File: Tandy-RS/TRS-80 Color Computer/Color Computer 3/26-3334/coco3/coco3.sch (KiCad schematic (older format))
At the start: 5 parts, among them CN1 Conn_02x20_Odd_Even

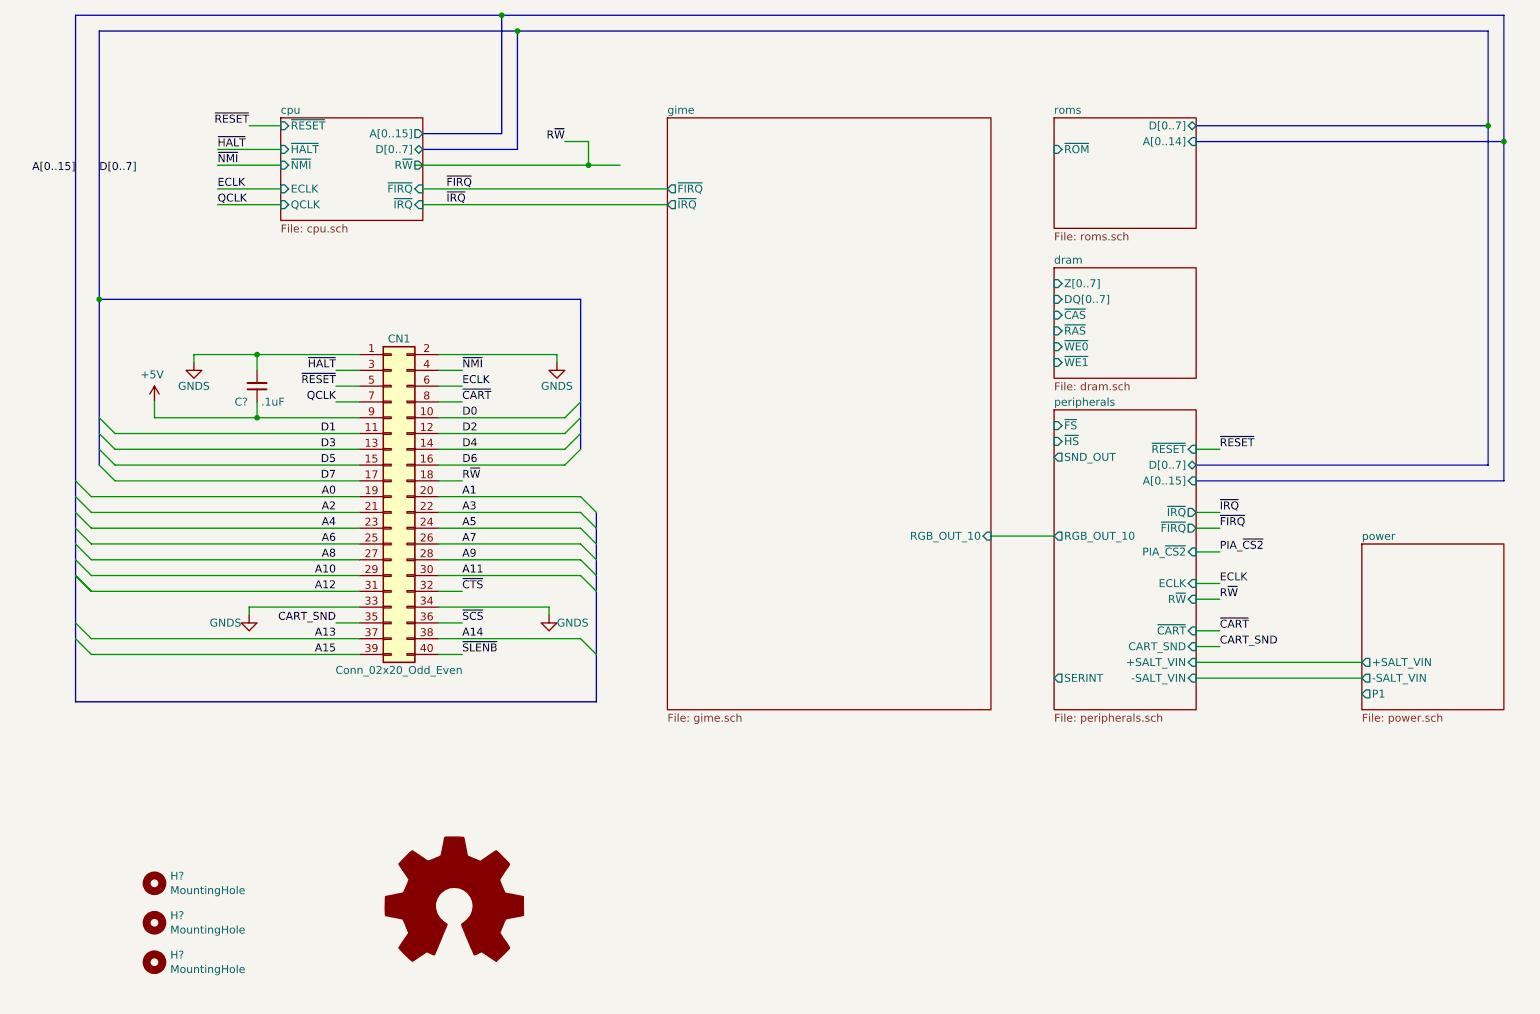
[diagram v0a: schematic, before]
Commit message: finished GIME section
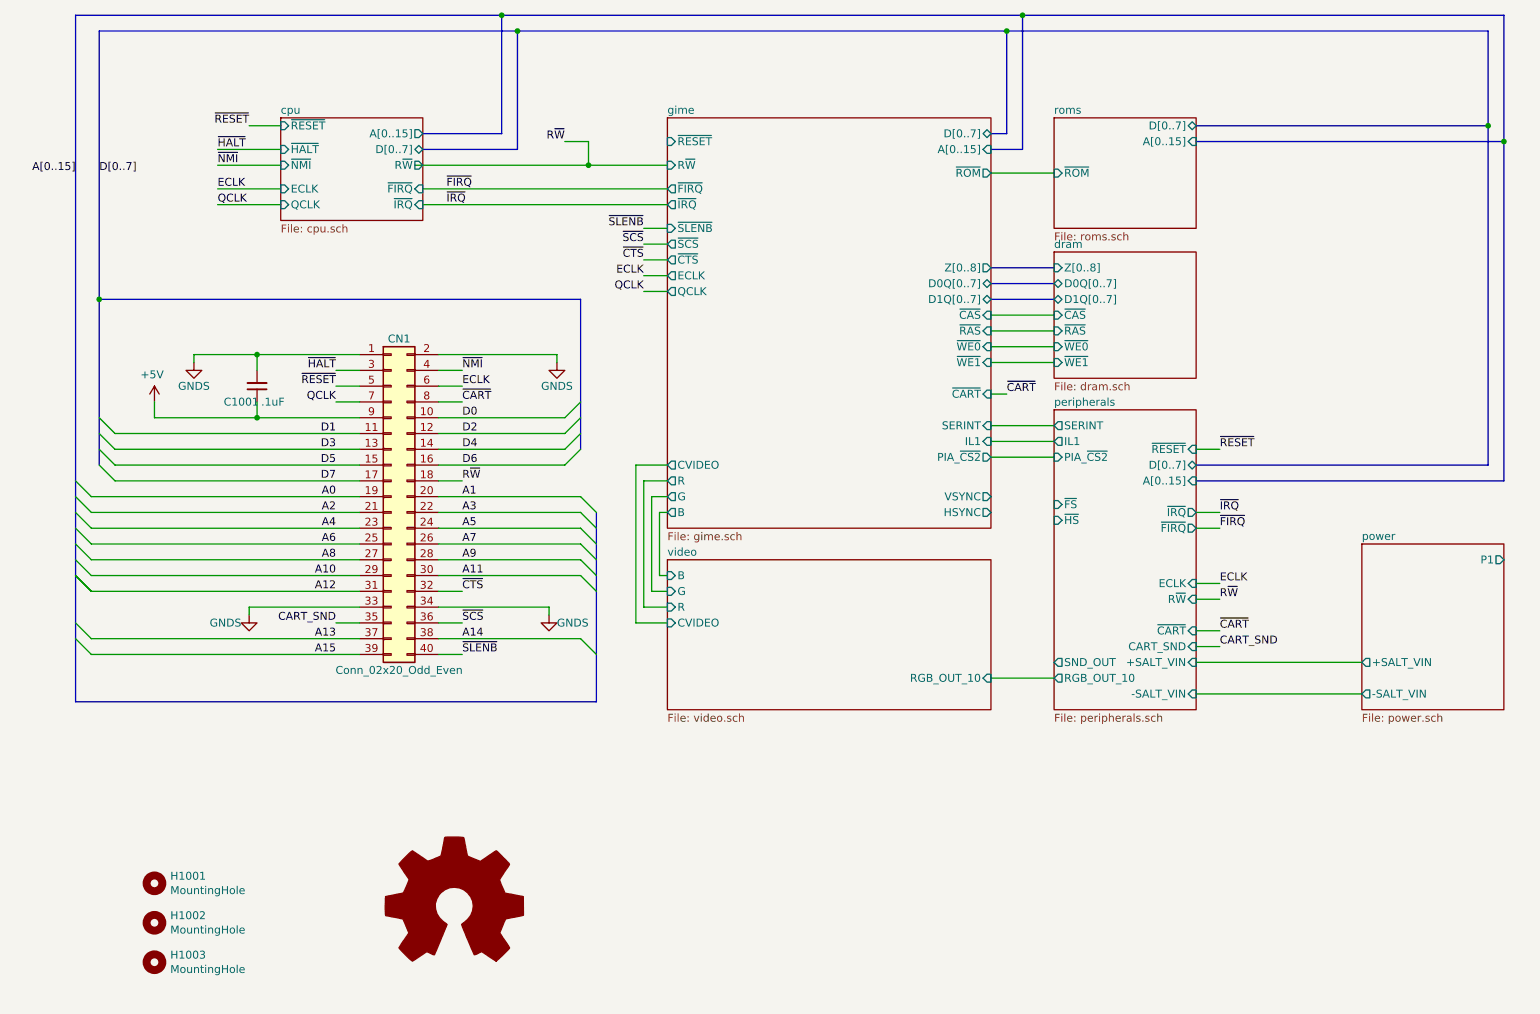
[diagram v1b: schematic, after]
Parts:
- gave numbers to parts that had none: 4
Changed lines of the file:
@@
 $Descr A 11000 8500
 encoding utf-8
-Sheet 1 7
+Sheet 1 8
 Title "TRS-80 Color Computer 3 (26-3334)"
 Date "2021-07-06"
@@
 $EndDescr
 $Sheet
-S 7050 3050 900  700
+S 7050 2950 900  800
 U 603E4732
 F0 "dram" 50
@@
 F2 "~RAS" I L 7050 3450 50
 F3 "~CAS" I L 7050 3350 50
-F4 "DQ[0..7]" I L 7050 3250 50
-F5 "Z[0..7]" I L 7050 3150 50
-F6 "~WE0" I L 7050 3550 50
-F7 "~WE1" I L 7050 3650 50
+F4 "~WE0" I L 7050 3550 50
+F5 "~WE1" I L 7050 3650 50
+F6 "Z[0..8]" I L 7050 3050 50
+F7 "D0Q[0..7]" B L 7050 3150 50
+F8 "D1Q[0..7]" B L 7050 3250 50
 $EndSheet
 $Sheet
@@
 F0 "roms" 50
 F1 "roms.sch" 50
-F2 "A[0..14]" I R 7950 2250 50
-F3 "D[0..7]" B R 7950 2150 50
-F4 "~ROM" I L 7050 2300 50
+F2 "D[0..7]" B R 7950 2150 50
+F3 "~ROM" I L 7050 2450 50
+F4 "A[0..15]" I R 7950 2250 50
 $EndSheet
 $Sheet
@@
 AR Path="/603E4732/60A48794" Ref="#PWR?"  Part="1"
 AR Path="/603D345E/60A48794" Ref="#PWR?"  Part="1"
-AR Path="/60A48794" Ref="#PWR?"  Part="1"
-F 0 "#PWR?" H 1600 3400 50  0001 C CNN
+AR Path="/60A48794" Ref="#PWR01001"  Part="1"
+F 0 "#PWR01001" H 1600 3400 50  0001 C CNN
 F 1 "GNDS" H 1600 3500 50  0000 C CNN
 F 2 "" H 1600 3650 50  0001 C CNN
@@
 AR Path="/603E4732/60A3AC34" Ref="#PWR?"  Part="1"
 AR Path="/603D345E/60A3AC34" Ref="#PWR?"  Part="1"
-AR Path="/60A3AC34" Ref="#PWR?"  Part="1"
-F 0 "#PWR?" H 3900 3400 50  0001 C CNN
+AR Path="/60A3AC34" Ref="#PWR01002"  Part="1"
+F 0 "#PWR01002" H 3900 3400 50  0001 C CNN
 F 1 "GNDS" H 3900 3500 50  0000 C CNN
 F 2 "" H 3900 3650 50  0001 C CNN
@@
 AR Path="/603E4732/60A24DD1" Ref="#PWR?"  Part="1"
 AR Path="/603D345E/60A24DD1" Ref="#PWR?"  Part="1"
-AR Path="/60A24DD1" Ref="#PWR?"  Part="1"
-F 0 "#PWR?" H 3850 5000 50  0001 C CNN
+AR Path="/60A24DD1" Ref="#PWR01005"  Part="1"
+F 0 "#PWR01005" H 3850 5000 50  0001 C CNN
 F 1 "GNDS" H 3700 5200 50  0000 C CNN
 F 2 "" H 3850 5250 50  0001 C CNN
@@
 AR Path="/603E4732/60A1FE63" Ref="#PWR?"  Part="1"
 AR Path="/603D345E/60A1FE63" Ref="#PWR?"  Part="1"
-AR Path="/60A1FE63" Ref="#PWR?"  Part="1"
-F 0 "#PWR?" H 1950 5000 50  0001 C CNN
+AR Path="/60A1FE63" Ref="#PWR01004"  Part="1"
+F 0 "#PWR01004" H 1950 5000 50  0001 C CNN
 F 1 "GNDS" H 1800 5200 50  0000 C CNN
 F 2 "" H 1950 5250 50  0001 C CNN
@@
 P 2000 3800
 AR Path="/60273794/6093C001" Ref="C?"  Part="1"
-AR Path="/6093C001" Ref="C?"  Part="1"
-F 0 "C?" H 2100 3900 50  0000 C CNN
+AR Path="/6093C001" Ref="C1001"  Part="1"
+F 0 "C1001" H 2100 3900 50  0000 C CNN
 F 1 ".1uF" H 1900 3900 50  0000 C CNN
 F 2 "Capacitor_THT:C_Disc_D4.7mm_W2.5mm_P5.00mm" H 2000 3800 50  0001 C CNN
@@
 P 1350 3900
 AR Path="/60273794/6093BFF7" Ref="#PWR?"  Part="1"
-AR Path="/6093BFF7" Ref="#PWR?"  Part="1"
-F 0 "#PWR?" H 1350 3750 50  0001 C CNN
+AR Path="/6093BFF7" Ref="#PWR01003"  Part="1"
+F 0 "#PWR01003" H 1350 3750 50  0001 C CNN
 F 1 "+5V" H 1365 4073 50  0000 C CNN
 F 2 "" H 1350 3900 50  0001 C CNN
@@
 F0 "power" 50
 F1 "power.sch" 50
-F2 "-SALT_VIN" O L 9000 5650 50
+F2 "-SALT_VIN" O L 9000 5750 50
 F3 "+SALT_VIN" O L 9000 5550 50
-F4 "P1" O L 9000 5750 50
+F4 "P1" O R 9900 4900 50
 $EndSheet
 Wire Bus Line
@@
 	7950 5550 9000 5550
 Wire Wire Line
-	9000 5650 7950 5650
+	9000 5750 7950 5750
 Wire Wire Line
 	2150 2150 1950 2150
 $Comp
-L Mechanical:MountingHole H?
+L Mechanical:MountingHole H1001
 U 1 1 60AD1126
 P 1350 6950
-F 0 "H?" H 1450 6996 50  0000 L CNN
+F 0 "H1001" H 1450 6996 50  0000 L CNN
 F 1 "MountingHole" H 1450 6905 50  0000 L CNN
 F 2 "MountingHole:MountingHole_4.5mm" H 1350 6950 50  0001 C CNN
@@
 $EndComp
 $Comp
-L Mechanical:MountingHole H?
+L Mechanical:MountingHole H1002
 U 1 1 60AD16B9
 P 1350 7200
-F 0 "H?" H 1450 7246 50  0000 L CNN
+F 0 "H1002" H 1450 7246 50  0000 L CNN
 F 1 "MountingHole" H 1450 7155 50  0000 L CNN
 F 2 "MountingHole:MountingHole_4mm" H 1350 7200 50  0001 C CNN
@@
 $EndComp
 $Comp
-L Mechanical:MountingHole H?
+L Mechanical:MountingHole H1003
 U 1 1 60AD74E1
 P 1350 7450
-F 0 "H?" H 1450 7496 50  0000 L CNN
+F 0 "H1003" H 1450 7496 50  0000 L CNN
 F 1 "MountingHole" H 1450 7405 50  0000 L CNN
 F 2 "MountingHole:MountingHole_4mm" H 1350 7450 50  0001 C CNN
@@
 $EndComp
 $Comp
-L Graphic:Logo_Open_Hardware_Large #LOGO?
+L Graphic:Logo_Open_Hardware_Large #LOGO1001
 U 1 1 608347FD
 P 3250 7100
-F 0 "#LOGO?" H 3250 7600 50  0001 C CNN
+F 0 "#LOGO1001" H 3250 7600 50  0001 C CNN
 F 1 "Logo_Open_Hardware_Large" H 3250 6700 50  0001 C CNN
 F 2 "" H 3250 7100 50  0001 C CNN
@@
 F0 "peripherals" 50
 F1 "peripherals.sch" 50
-F2 "-SALT_VIN" I R 7950 5650 50
+F2 "-SALT_VIN" I R 7950 5750 50
 F3 "+SALT_VIN" I R 7950 5550 50
 F4 "D[0..7]" B R 7950 4300 50
@@
 F7 "~RESET" I R 7950 4200 50
 F8 "A[0..15]" I R 7950 4400 50
-F9 "~HS" I L 7050 4150 50
+F9 "~HS" I L 7050 4650 50
 F10 "~CART" I R 7950 5350 50
-F11 "SND_OUT" O L 7050 4250 50
+F11 "SND_OUT" O L 7050 5550 50
 F12 "CART_SND" I R 7950 5450 50
 F13 "~FIRQ" O R 7950 4700 50
-F14 "~FS" I L 7050 4050 50
-F15 "SERINT" O L 7050 5650 50
-F16 "RGB_OUT_10" O L 7050 4750 50
-F17 "PIA_~CS2" I R 7950 4850 50
+F14 "~FS" I L 7050 4550 50
+F15 "SERINT" O L 7050 4050 50
+F16 "RGB_OUT_10" O L 7050 5650 50
+F17 "PIA_~CS2" I L 7050 4250 50
 F18 "ECLK" I R 7950 5050 50
+F19 "IL1" O L 7050 4150 50
 $EndSheet
-Text Label 8100 4850 0    50   ~ 0
-PIA_~CS2
-Wire Wire Line
-	7950 4850 8100 4850
 $Sheet
-S 4600 2100 2050 3750
+S 4600 2100 2050 2600
 U 61257512
 F0 "gime" 50
 F1 "gime.sch" 50
-F2 "RGB_OUT_10" I R 6650 4750 50
-F3 "~IRQ" O L 4600 2650 50
-F4 "~FIRQ" O L 4600 2550 50
+F2 "~IRQ" O L 4600 2650 50
+F3 "~FIRQ" O L 4600 2550 50
+F4 "~WE0" I R 6650 3550 50
+F5 "~WE1" I R 6650 3650 50
+F6 "~RESET" I L 4600 2250 50
+F7 "R~W" I L 4600 2400 50
+F8 "~CAS" I R 6650 3350 50
+F9 "~RAS" I R 6650 3450 50
+F10 "D0Q[0..7]" B R 6650 3150 50
+F11 "D1Q[0..7]" B R 6650 3250 50
+F12 "Z[0..8]" O R 6650 3050 50
+F13 "D[0..7]" B R 6650 2200 50
+F14 "A[0..15]" I R 6650 2300 50
+F15 "R" O L 4600 4400 50
+F16 "G" O L 4600 4500 50
+F17 "B" O L 4600 4600 50
+F18 "CVIDEO" O L 4600 4300 50
+F19 "SERINT" I R 6650 4050 50
+F20 "IL1" I R 6650 4150 50
+F21 "~CART" I R 6650 3850 50
+F22 "~SLENB" I L 4600 2800 50
+F23 "~SCS" O L 4600 2900 50
+F24 "~CTS" O L 4600 3000 50
+F25 "~ROM" O R 6650 2450 50
+F26 "PIA_~CS2" O R 6650 4250 50
+F27 "ECLK" O L 4600 3100 50
+F28 "QCLK" O L 4600 3200 50
+F29 "VSYNC" O R 6650 4500 50
+F30 "HSYNC" O R 6650 4600 50
 $EndSheet
 Wire Bus Line
@@
 R~W
 Wire Bus Line
-	3550 1450 9900 1450
-Wire Bus Line
-	3650 1550 9800 1550
+	3550 1450 6850 1450
+Wire Bus Line
+	3650 1550 6750 1550
 Wire Wire Line
 	3000 2400 4100 2400
@@
 Connection ~ 4100 2400
 Wire Wire Line
-	4100 2400 4300 2400
-Wire Wire Line
 	3050 2550 4600 2550
 Wire Wire Line
 	3050 2650 4600 2650
-Wire Wire Line
-	7050 4750 6650 4750
+Wire Bus Line
+	6650 3150 7050 3150
+Wire Wire Line
+	6650 3550 7050 3550
+Wire Wire Line
+	7050 3650 6650 3650
+Wire Bus Line
+	7050 3250 6650 3250
+Wire Wire Line
+	4100 2400 4600 2400
+Wire Wire Line
+	6650 3350 7050 3350
+Wire Wire Line
+	7050 3450 6650 3450
+Wire Bus Line
+	6650 3050 7050 3050
+Wire Bus Line
+	6650 2200 6750 2200
+Wire Bus Line
+	6750 2200 6750 1550
+Connection ~ 6750 1550
+Wire Bus Line
+	6750 1550 9800 1550
+Wire Bus Line
+	6650 2300 6850 2300
+Wire Bus Line
+	6850 2300 6850 1450
+Connection ~ 6850 1450
+Wire Bus Line
+	6850 1450 9900 1450
+$Sheet
+S 4600 4900 2050 950
+U 612A4892
+F0 "video" 50
+F1 "video.sch" 50
+F2 "RGB_OUT_10" I R 6650 5650 50
+F3 "CVIDEO" I L 4600 5300 50
+F4 "R" I L 4600 5200 50
+F5 "G" I L 4600 5100 50
+F6 "B" I L 4600 5000 50
+$EndSheet
+Wire Wire Line
+	7050 5650 6650 5650
+Wire Wire Line
+	4600 4600 4550 4600
+Wire Wire Line
+	4550 4600 4550 5000
+Wire Wire Line
+	4550 5000 4600 5000
+Wire Wire Line
+	4600 4500 4500 4500
+Wire Wire Line
+	4500 4500 4500 5100
+Wire Wire Line
+	4500 5100 4600 5100
+Wire Wire Line
+	4600 4400 4450 4400
+Wire Wire Line
+	4450 4400 4450 5200
+Wire Wire Line
+	4450 5200 4600 5200
+Wire Wire Line
+	4600 4300 4400 4300
+Wire Wire Line
+	4400 4300 4400 5300
+Wire Wire Line
+	4400 5300 4600 5300
+Wire Wire Line
+	7050 4050 6650 4050
+Wire Wire Line
+	7050 4150 6650 4150
+Text Label 6750 3850 0    50   ~ 0
+~CART
+Wire Wire Line
+	6750 3850 6650 3850
+Wire Wire Line
+	7050 4250 6650 4250
+Wire Wire Line
+	6650 2450 7050 2450
+Text Label 4450 2800 2    50   ~ 0
+~SLENB
+Wire Wire Line
+	4600 2800 4450 2800
+Text Label 4450 2900 2    50   ~ 0
+~SCS
+Text Label 4450 3000 2    50   ~ 0
+~CTS
+Wire Wire Line
+	4600 2900 4450 2900
+Wire Wire Line
+	4450 3000 4600 3000
+Text Label 4450 3100 2    50   ~ 0
+ECLK
+Wire Wire Line
+	4600 3100 4450 3100
+Text Label 4450 3200 2    50   ~ 0
+QCLK
+Wire Wire Line
+	4600 3200 4450 3200
 Wire Bus Line
 	1000 3250 1000 4300
